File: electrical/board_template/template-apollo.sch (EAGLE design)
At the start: 2 parts

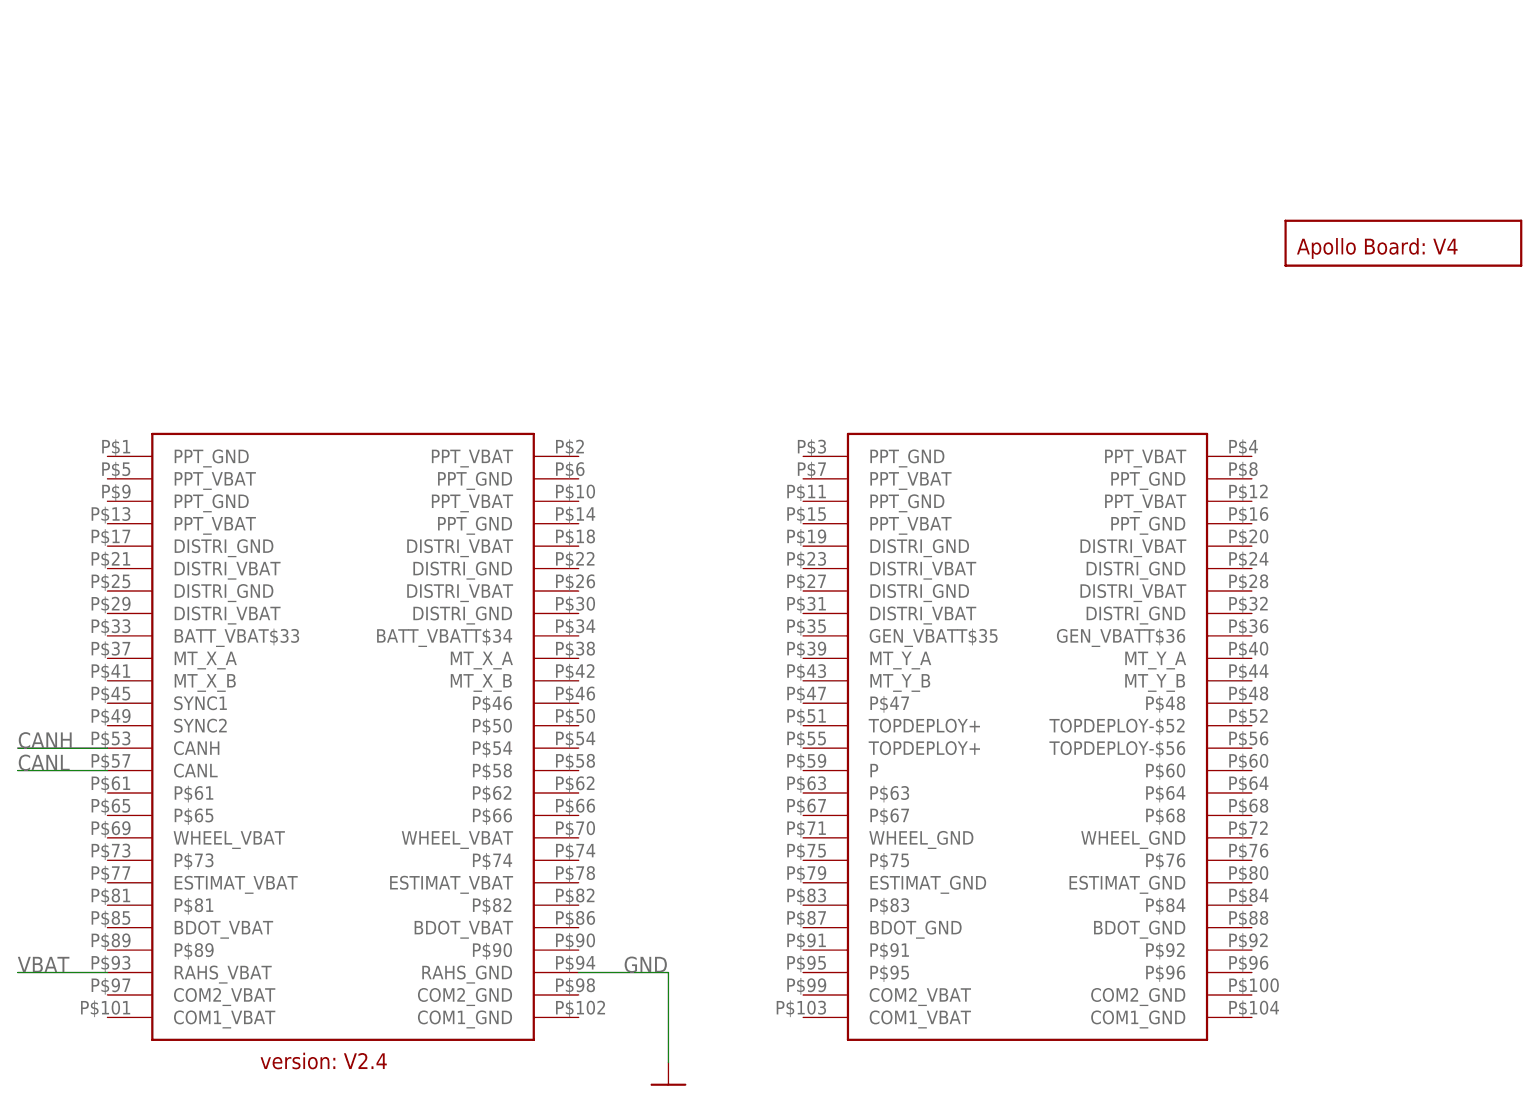
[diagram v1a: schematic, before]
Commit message: fix template board symbols
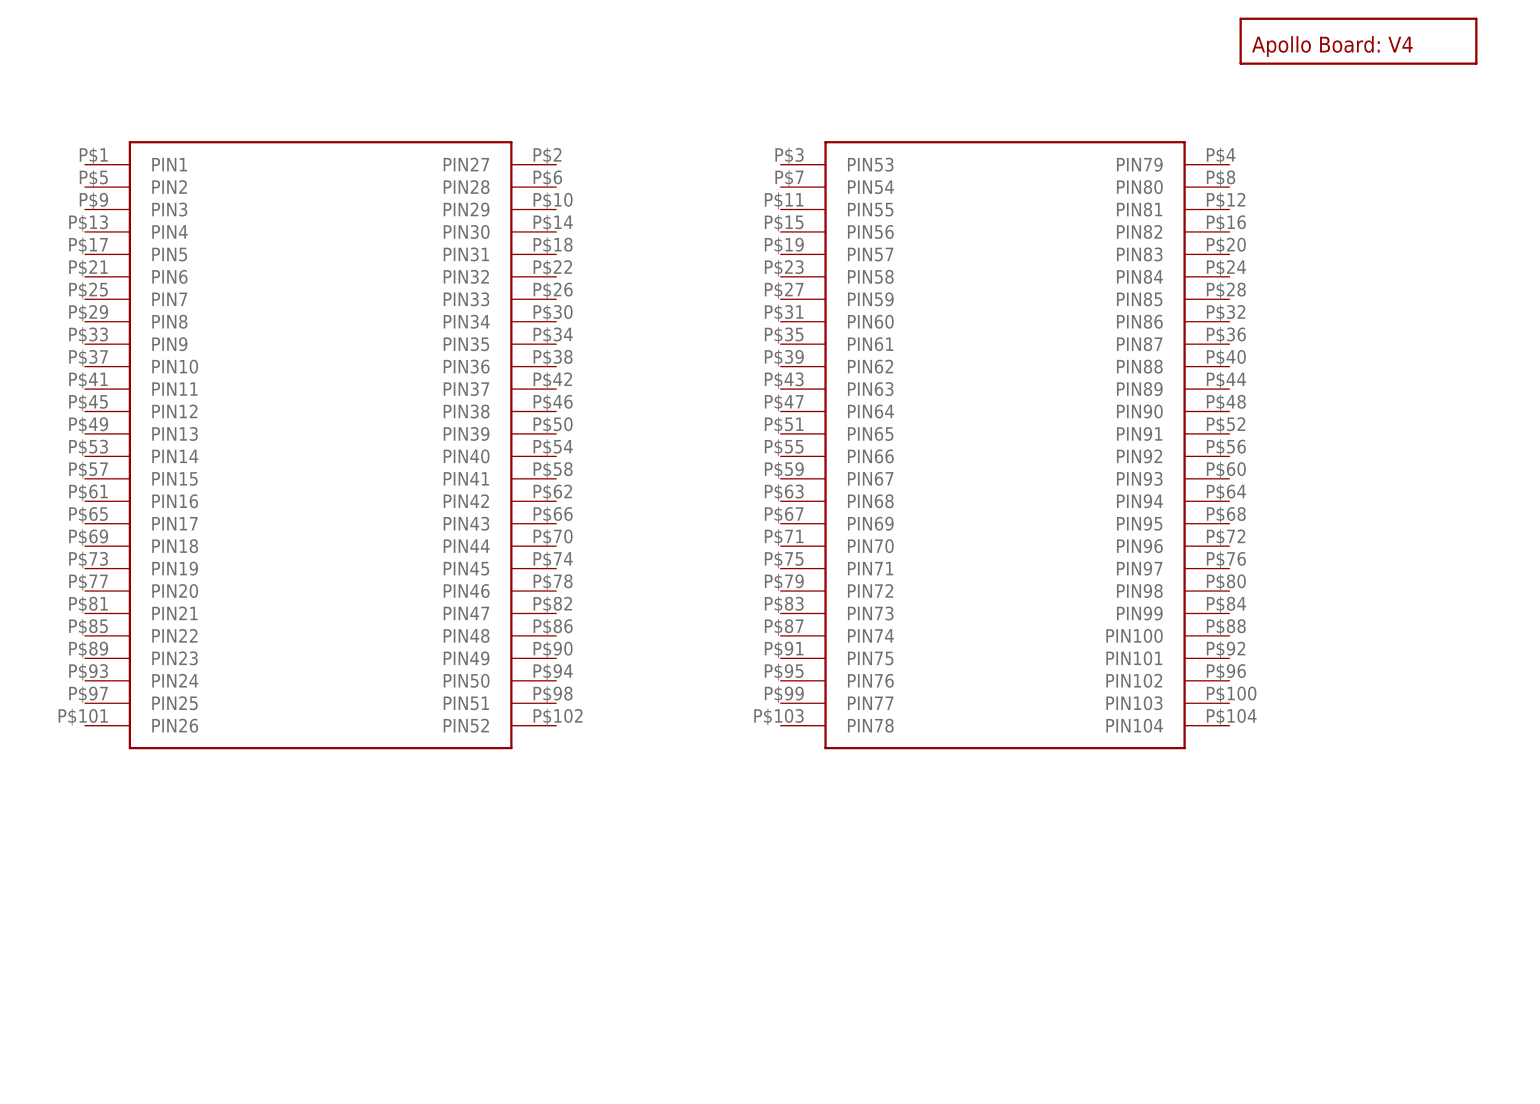
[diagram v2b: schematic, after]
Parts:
- removed JP1: PC104_CONNECTOR, DubSat1 Components latest:PC104_CONNECTOR
- added U$2: PC104_CONNECTOR, template_board:PC104_CONNECTOR
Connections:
- removed net CANH: JP1.CANH
- removed net CANL: JP1.CANL
- removed net GND: JP1.RAHS_GND@94
- removed net VBAT: JP1.RAHS_VBAT@93
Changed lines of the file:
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@@
 <grid distance="0.1" unitdist="inch" unit="inch" style="lines" multiple="1" display="no" altdistance="0.01" altunitdist="inch" altunit="inch"/>
 <layers>
-<layer number="1" name="Top" color="4" fill="1" visible="yes" active="no"/>
-<layer number="2" name="Route2" color="1" fill="3" visible="yes" active="no"/>
-<layer number="3" name="Route3" color="4" fill="3" visible="yes" active="no"/>
-<layer number="4" name="Route4" color="1" fill="4" visible="yes" active="no"/>
-<layer number="5" name="Route5" color="4" fill="4" visible="yes" active="no"/>
-<layer number="6" name="Route6" color="1" fill="8" visible="yes" active="no"/>
-<layer number="7" name="Route7" color="4" fill="8" visible="yes" active="no"/>
-<layer number="8" name="Route8" color="1" fill="2" visible="yes" active="no"/>
-<layer number="9" name="Route9" color="4" fill="2" visible="yes" active="no"/>
-<layer number="10" name="Route10" color="1" fill="7" visible="yes" active="no"/>
-<layer number="11" name="Route11" color="4" fill="7" visible="yes" active="no"/>
-<layer number="12" name="Route12" color="1" fill="5" visible="yes" active="no"/>
-<layer number="13" name="Route13" color="4" fill="5" visible="yes" active="no"/>
-<layer number="14" name="Route14" color="1" fill="6" visible="yes" active="no"/>
-<layer number="15" name="Route15" color="4" fill="6" visible="yes" active="no"/>
-<layer number="16" name="Bottom" color="1" fill="1" visible="yes" active="no"/>
-<layer number="17" name="Pads" color="2" fill="1" visible="yes" active="no"/>
-<layer number="18" name="Vias" color="2" fill="1" visible="yes" active="no"/>
-<layer number="19" name="Unrouted" color="6" fill="1" visible="yes" active="no"/>
-<layer number="20" name="Dimension" color="15" fill="1" visible="yes" active="no"/>
-<layer number="21" name="tPlace" color="7" fill="1" visible="yes" active="no"/>
-<layer number="22" name="bPlace" color="7" fill="1" visible="yes" active="no"/>
-<layer number="23" name="tOrigins" color="15" fill="1" visible="yes" active="no"/>
-<layer number="24" name="bOrigins" color="15" fill="1" visible="yes" active="no"/>
-<layer number="25" name="tNames" color="7" fill="1" visible="yes" active="no"/>
-<layer number="26" name="bNames" color="7" fill="1" visible="yes" active="no"/>
-<layer number="27" name="tValues" color="7" fill="1" visible="yes" active="no"/>
-<layer number="28" name="bValues" color="7" fill="1" visible="yes" active="no"/>
+<layer number="1" name="Top" color="4" fill="1" visible="no" active="no"/>
+<layer number="2" name="Route2" color="1" fill="3" visible="no" active="no"/>
+<layer number="3" name="Route3" color="4" fill="3" visible="no" active="no"/>
+<layer number="4" name="Route4" color="1" fill="4" visible="no" active="no"/>
+<layer number="5" name="Route5" color="4" fill="4" visible="no" active="no"/>
+<layer number="6" name="Route6" color="1" fill="8" visible="no" active="no"/>
+<layer number="7" name="Route7" color="4" fill="8" visible="no" active="no"/>
+<layer number="8" name="Route8" color="1" fill="2" visible="no" active="no"/>
+<layer number="9" name="Route9" color="4" fill="2" visible="no" active="no"/>
+<layer number="10" name="Route10" color="1" fill="7" visible="no" active="no"/>
+<layer number="11" name="Route11" color="4" fill="7" visible="no" active="no"/>
+<layer number="12" name="Route12" color="1" fill="5" visible="no" active="no"/>
+<layer number="13" name="Route13" color="4" fill="5" visible="no" active="no"/>
+<layer number="14" name="Route14" color="1" fill="6" visible="no" active="no"/>
+<layer number="15" name="Route15" color="4" fill="6" visible="no" active="no"/>
+<layer number="16" name="Bottom" color="1" fill="1" visible="no" active="no"/>
+<layer number="17" name="Pads" color="2" fill="1" visible="no" active="no"/>
+<layer number="18" name="Vias" color="2" fill="1" visible="no" active="no"/>
+<layer number="19" name="Unrouted" color="6" fill="1" visible="no" active="no"/>
+<layer number="20" name="Dimension" color="15" fill="1" visible="no" active="no"/>
+<layer number="21" name="tPlace" color="7" fill="1" visible="no" active="no"/>
+<layer number="22" name="bPlace" color="7" fill="1" visible="no" active="no"/>
+<layer number="23" name="tOrigins" color="15" fill="1" visible="no" active="no"/>
+<layer number="24" name="bOrigins" color="15" fill="1" visible="no" active="no"/>
+<layer number="25" name="tNames" color="7" fill="1" visible="no" active="no"/>
+<layer number="26" name="bNames" color="7" fill="1" visible="no" active="no"/>
+<layer number="27" name="tValues" color="7" fill="1" visible="no" active="no"/>
+<layer number="28" name="bValues" color="7" fill="1" visible="no" active="no"/>
 <layer number="29" name="tStop" color="7" fill="3" visible="no" active="no"/>
 <layer number="30" name="bStop" color="7" fill="6" visible="no" active="no"/>
@@
 <layer number="35" name="tGlue" color="7" fill="4" visible="no" active="no"/>
 <layer number="36" name="bGlue" color="7" fill="5" visible="no" active="no"/>
-<layer number="37" name="tTest" color="7" fill="1" visible="yes" active="no"/>
-<layer number="38" name="bTest" color="7" fill="1" visible="yes" active="no"/>
+<layer number="37" name="tTest" color="7" fill="1" visible="no" active="no"/>
+<layer number="38" name="bTest" color="7" fill="1" visible="no" active="no"/>
 <layer number="39" name="tKeepout" color="4" fill="11" visible="no" active="no"/>
 <layer number="40" name="bKeepout" color="1" fill="11" visible="no" active="no"/>
@@
 <layer number="44" name="Drills" color="7" fill="1" visible="no" active="no"/>
 <layer number="45" name="Holes" color="7" fill="1" visible="no" active="no"/>
-<layer number="46" name="Milling" color="3" fill="1" visible="yes" active="no"/>
-<layer number="47" name="Measures" color="7" fill="1" visible="yes" active="no"/>
-<layer number="48" name="Document" color="7" fill="1" visible="yes" active="no"/>
-<layer number="49" name="Reference" color="7" fill="1" visible="yes" active="no"/>
-<layer number="50" name="dxf" color="7" fill="1" visible="yes" active="no"/>
-<layer number="51" name="tDocu" color="7" fill="1" visible="yes" active="no"/>
-<layer number="52" name="bDocu" color="7" fill="1" visible="yes" active="no"/>
-<layer number="53" name="tGND_GNDA" color="7" fill="9" visible="yes" active="no"/>
-<layer number="54" name="bGND_GNDA" color="1" fill="9" visible="yes" active="no"/>
-<layer number="56" name="wert" color="7" fill="1" visible="yes" active="no"/>
-<layer number="57" name="tCAD" color="7" fill="1" visible="yes" active="no"/>
-<layer number="58" name="bCAD" color="11" fill="1" visible="yes" active="no"/>
-<layer number="59" name="tCarbon" color="7" fill="1" visible="yes" active="no"/>
-<layer number="60" name="bCarbon" color="7" fill="1" visible="yes" active="no"/>
+<layer number="46" name="Milling" color="3" fill="1" visible="no" active="no"/>
+<layer number="47" name="Measures" color="7" fill="1" visible="no" active="no"/>
+<layer number="48" name="Document" color="7" fill="1" visible="no" active="no"/>
+<layer number="49" name="Reference" color="7" fill="1" visible="no" active="no"/>
+<layer number="50" name="dxf" color="7" fill="1" visible="no" active="no"/>
+<layer number="51" name="tDocu" color="7" fill="1" visible="no" active="no"/>
+<layer number="52" name="bDocu" color="7" fill="1" visible="no" active="no"/>
+<layer number="53" name="tGND_GNDA" color="7" fill="9" visible="no" active="no"/>
+<layer number="54" name="bGND_GNDA" color="1" fill="9" visible="no" active="no"/>
+<layer number="56" name="wert" color="7" fill="1" visible="no" active="no"/>
+<layer number="57" name="tCAD" color="7" fill="1" visible="no" active="no"/>
+<layer number="58" name="bCAD" color="11" fill="1" visible="no" active="no"/>
+<layer number="59" name="tCarbon" color="7" fill="1" visible="no" active="no"/>
+<layer number="60" name="bCarbon" color="7" fill="1" visible="no" active="no"/>
 <layer number="88" name="SimResults" color="9" fill="1" visible="yes" active="yes"/>
 <layer number="89" name="SimProbes" color="9" fill="1" visible="yes" active="yes"/>
@@
 </classes>
 <parts>
-<part name="JP1" library="DubSat1 Components latest" deviceset="PC104_CONNECTOR" device=""/>
-<part name="GND15" library="SparkFun-Aesthetics" deviceset="GND" device=""/>
 <part name="U$1" library="template_board" deviceset="BOARD_TEMPLATE" device="1"/>
+<part name="U$2" library="template_board" deviceset="PC104_CONNECTOR" device=""/>
 </parts>
 <sheets>
@@
 </plain>
 <instances>
-<instance part="JP1" gate="G$1" x="304.8" y="124.46" smashed="yes"/>
-<instance part="GND15" gate="1" x="302.26" y="83.82" smashed="yes"/>
-<instance part="U$1" gate="G$1" x="373.38" y="177.8" smashed="yes"/>
+<instance part="U$1" gate="G$1" x="368.3" y="200.66" smashed="yes"/>
+<instance part="U$2" gate="G$1" x="302.26" y="157.48" smashed="yes"/>
 </instances>
 <busses>
 </busses>
 <nets>
-<net name="GND" class="0">
-<segment>
-<wire x1="292.1" y1="96.52" x2="302.26" y2="96.52" width="0.1524" layer="91"/>
-<wire x1="302.26" y1="96.52" x2="302.26" y2="86.36" width="0.1524" layer="91"/>
-<pinref part="JP1" gate="G$1" pin="RAHS_GND@94"/>
-<pinref part="GND15" gate="1" pin="GND"/>
-<label x="297.18" y="96.52" size="1.778" layer="95"/>
-</segment>
-</net>
-<net name="CANL" class="0">
-<segment>
-<pinref part="JP1" gate="G$1" pin="CANL"/>
-<wire x1="228.6" y1="119.38" x2="238.76" y2="119.38" width="0.1524" layer="91"/>
-<label x="228.6" y="119.38" size="1.778" layer="95"/>
-</segment>
-</net>
-<net name="CANH" class="0">
-<segment>
-<pinref part="JP1" gate="G$1" pin="CANH"/>
-<wire x1="238.76" y1="121.92" x2="228.6" y2="121.92" width="0.1524" layer="91"/>
-<label x="228.6" y="121.92" size="1.778" layer="95"/>
-</segment>
-</net>
-<net name="VBAT" class="0">
-<segment>
-<pinref part="JP1" gate="G$1" pin="RAHS_VBAT@93"/>
-<wire x1="238.76" y1="96.52" x2="228.6" y2="96.52" width="0.1524" layer="91"/>
-<label x="228.6" y="96.52" size="1.778" layer="95"/>
-</segment>
-</net>
 </nets>
 </sheet>
